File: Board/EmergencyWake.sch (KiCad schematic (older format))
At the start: 129 parts, among them J1 USB_C_Receptacle_USB2.0, J2 Micro_SD_Card_Det, J3 Conn_01x03, J4 Conn_01x02, J5 Conn_01x04, J6 Conn_01x04, J7 Conn_01x02, J8 Conn_01x04, J9 Conn_01x04, Q1 AO3400A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

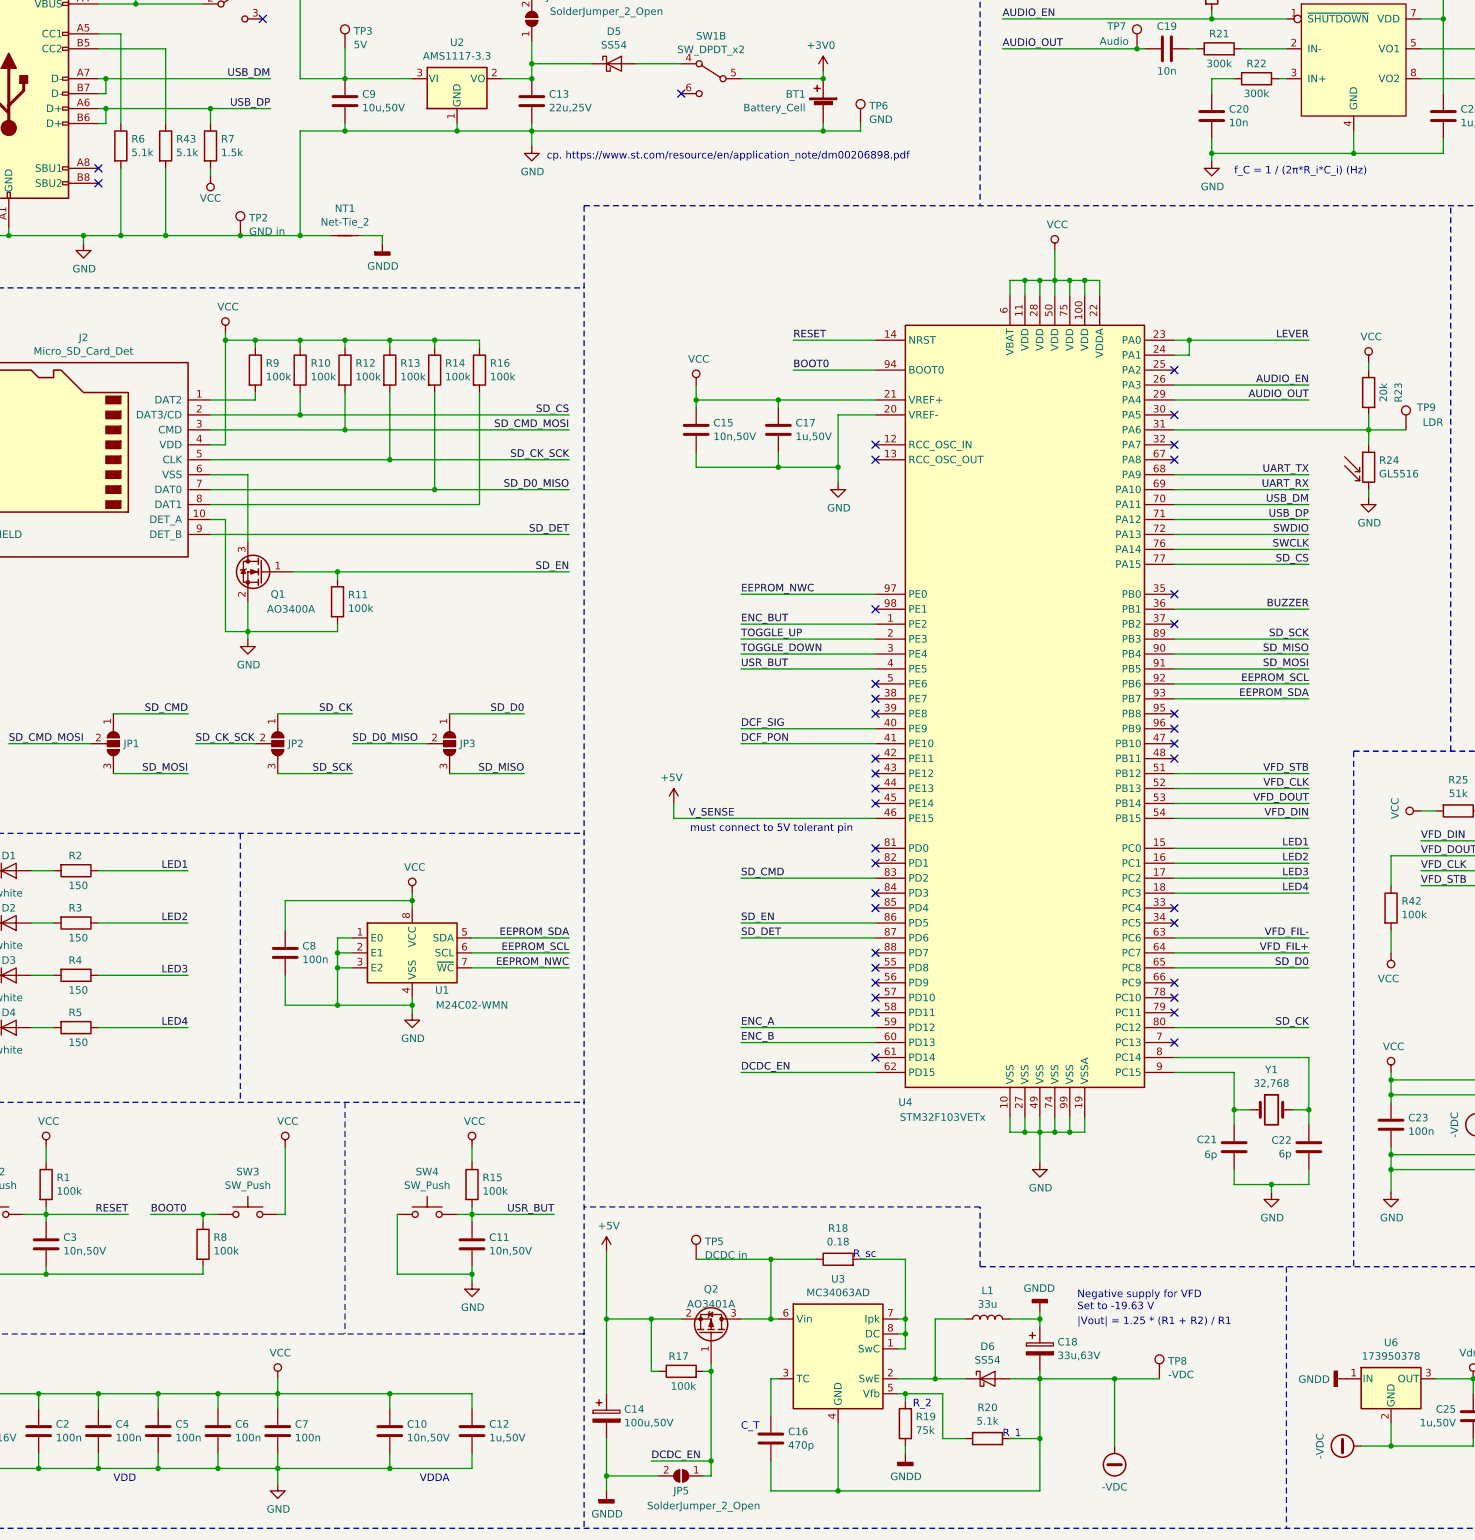
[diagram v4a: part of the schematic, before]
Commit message: [Board] Switched from F103 to F407
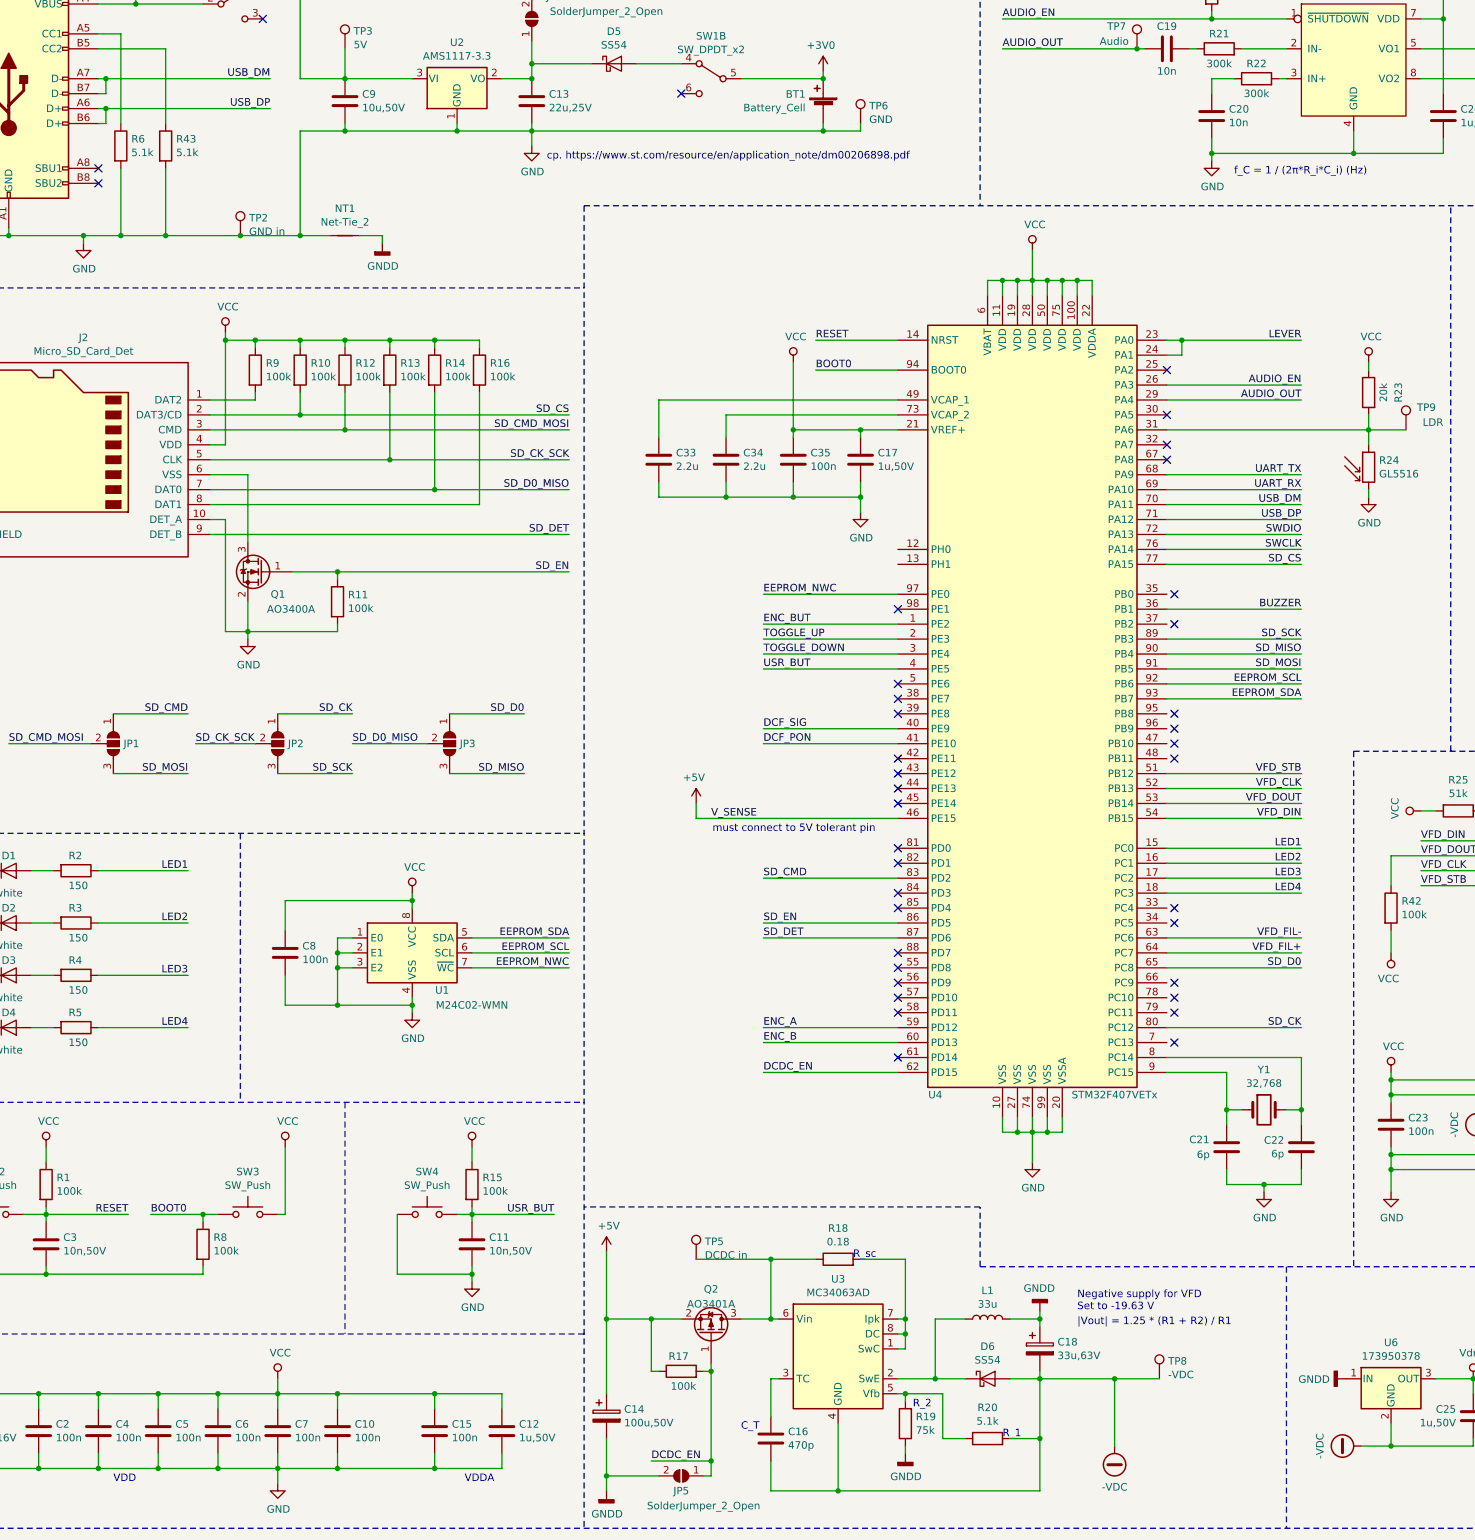
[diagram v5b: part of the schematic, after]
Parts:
- removed R7: 1.5k, Resistor_SMD:R_0603_1608Metric, symbol Device:R
- removed U4: STM32F103VETx, Package_QFP:LQFP-100_14x14mm_P0.5mm, symbol MCU_ST_STM32F1:STM32F103VETx
- added C33, C34: 2.2u, Capacitor_SMD:C_0603_1608Metric, symbol Device:C
- added C35: 100n, Capacitor_SMD:C_0402_1005Metric, symbol Device:C
- added U4: STM32F407VETx, Package_QFP:LQFP-100_14x14mm_P0.5mm, symbol MCU_ST_STM32F4:STM32F407VETx
- C10, C15: value 10n,50V -> 100n; LCSC C15195 -> C1525
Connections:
- net +5V: now also U4.46 (PE15)
- net AUDIO_EN: now also U4.26 (PA3)
- net AUDIO_OUT: now also U4.29 (PA4)
- net BOOT0: now also U4.94 (BOOT0)
- net BUZZER: now also U4.36 (PB1)
- net DCDC_EN: now also U4.62 (PD15)
- net DCF_PON: now also U4.41 (PE10)
- net DCF_SIG: now also U4.40 (PE9)
- net EEPROM_NWC: now also U4.97 (PE0)
- net EEPROM_SCL: now also U4.92 (PB6)
- net EEPROM_SDA: now also U4.93 (PB7)
- net ENC_A: now also U4.59 (PD12)
- net ENC_B: now also U4.60 (PD13)
- net ENC_BUT: now also U4.1 (PE2)
- net GND: now also C33.2, C34.2, C35.2, U4.10 (VSS), U4.20 (VSSA), U4.27 (VSS), U4.74 (VSS), U4.99 (VSS)
- net LED1: now also U4.15 (PC0)
- net LED2: now also U4.16 (PC1)
- net LED3: now also U4.17 (PC2)
- net LED4: now also U4.18 (PC3)
- net LEVER: now also U4.23 (PA0), U4.24 (PA1)
- net RESET: now also U4.14 (NRST)
- net SD_CK: now also U4.80 (PC12)
- net SD_CMD: now also U4.83 (PD2)
- net SD_CS: now also U4.77 (PA15)
- net SD_D0: now also U4.65 (PC8)
- net SD_DET: now also U4.87 (PD6)
- net SD_EN: now also U4.86 (PD5)
- net SD_MISO: now also U4.90 (PB4)
- net SD_MOSI: now also U4.91 (PB5)
- net SD_SCK: now also U4.89 (PB3)
- net SWCLK: now also U4.76 (PA14)
- net SWDIO: now also U4.72 (PA13)
- net TOGGLE_DOWN: now also U4.3 (PE4)
- net TOGGLE_UP: now also U4.2 (PE3)
- net UART_RX: now also U4.69 (PA10)
- net UART_TX: now also U4.68 (PA9)
- net USB_DM: now also U4.70 (PA11)
- net USB_DP: now also U4.71 (PA12)
- net USR_BUT: now also U4.4 (PE5)
- net VCC: now also C35.1, U4.100 (VDD), U4.11 (VDD), U4.19 (VDD), U4.21 (VREF+), U4.22 (VDDA), U4.28 (VDD), U4.50 (VDD), U4.6 (VBAT), U4.75 (VDD)
- net VFD_CLK: now also U4.52 (PB13)
- net VFD_DIN: now also U4.54 (PB15)
- net VFD_DOUT: now also U4.53 (PB14)
- net VFD_FIL+: now also U4.64 (PC7)
- net VFD_FIL-: now also U4.63 (PC6)
- net VFD_STB: now also U4.51 (PB12)
- net at R23.2, R24.1, TP9.1: now also U4.31 (PA6)
- net at C22.1, Y1.2: now also U4.8 (PC14)
- net at C21.1, Y1.1: now also U4.9 (PC15)
- new net: C33.1, U4.49 (VCAP_1)
- new net: C34.1, U4.73 (VCAP_2)
- no-connect marks 58 -> 56
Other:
- moved on the sheet: C12, C17, C21, C22, Y1

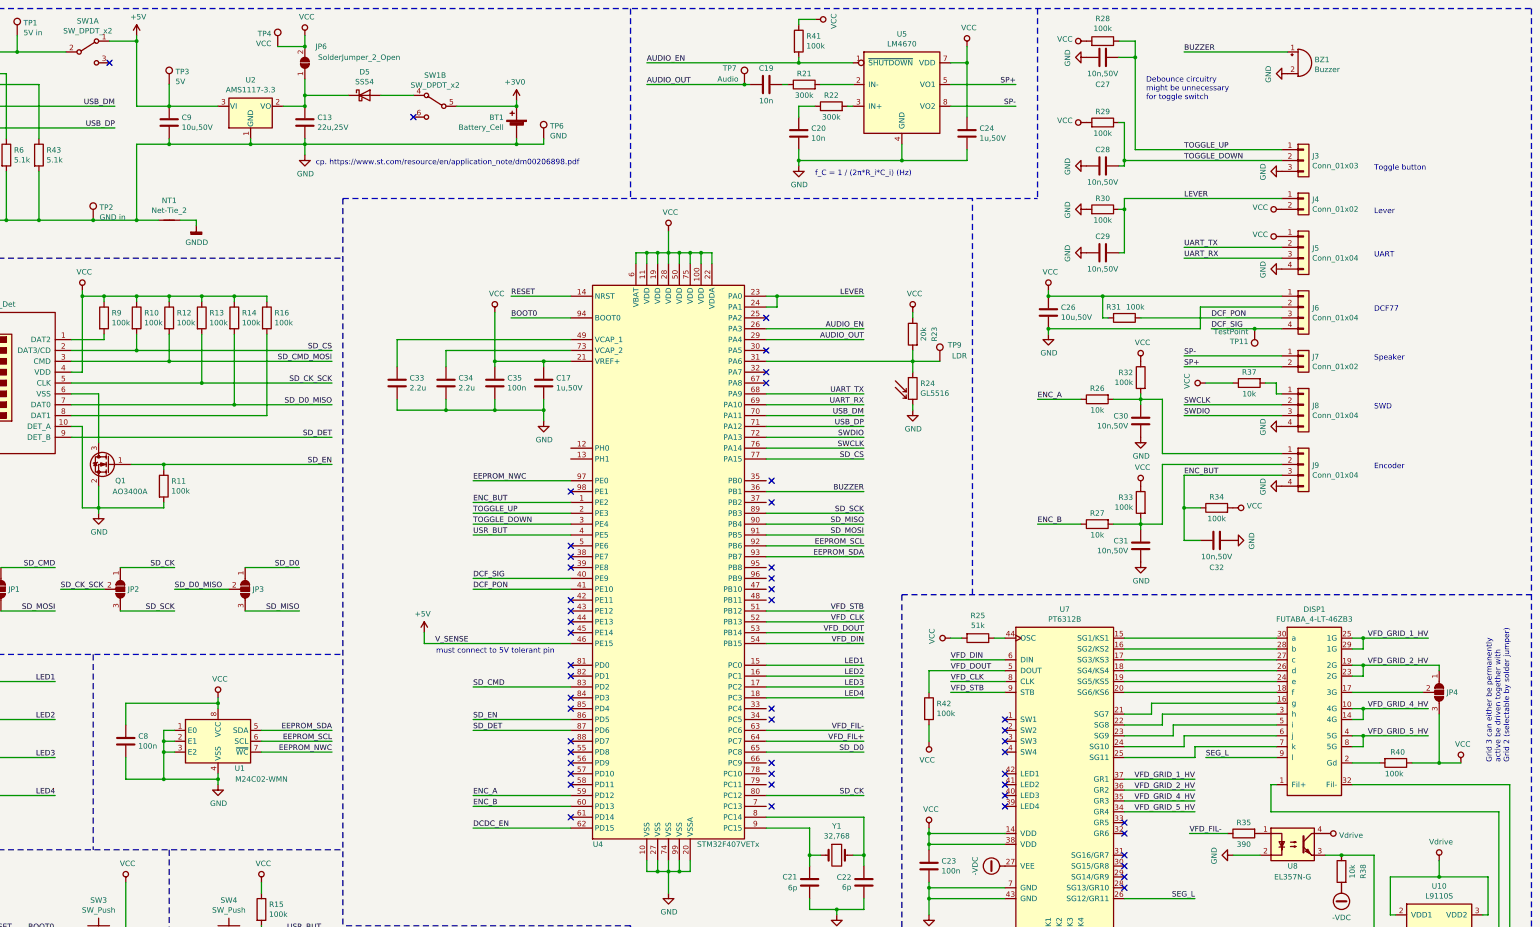
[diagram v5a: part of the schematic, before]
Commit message: [Board] Removed solder paste for not-fitted components. Added I2C for proximity sensor. Moved SWD and UART connector
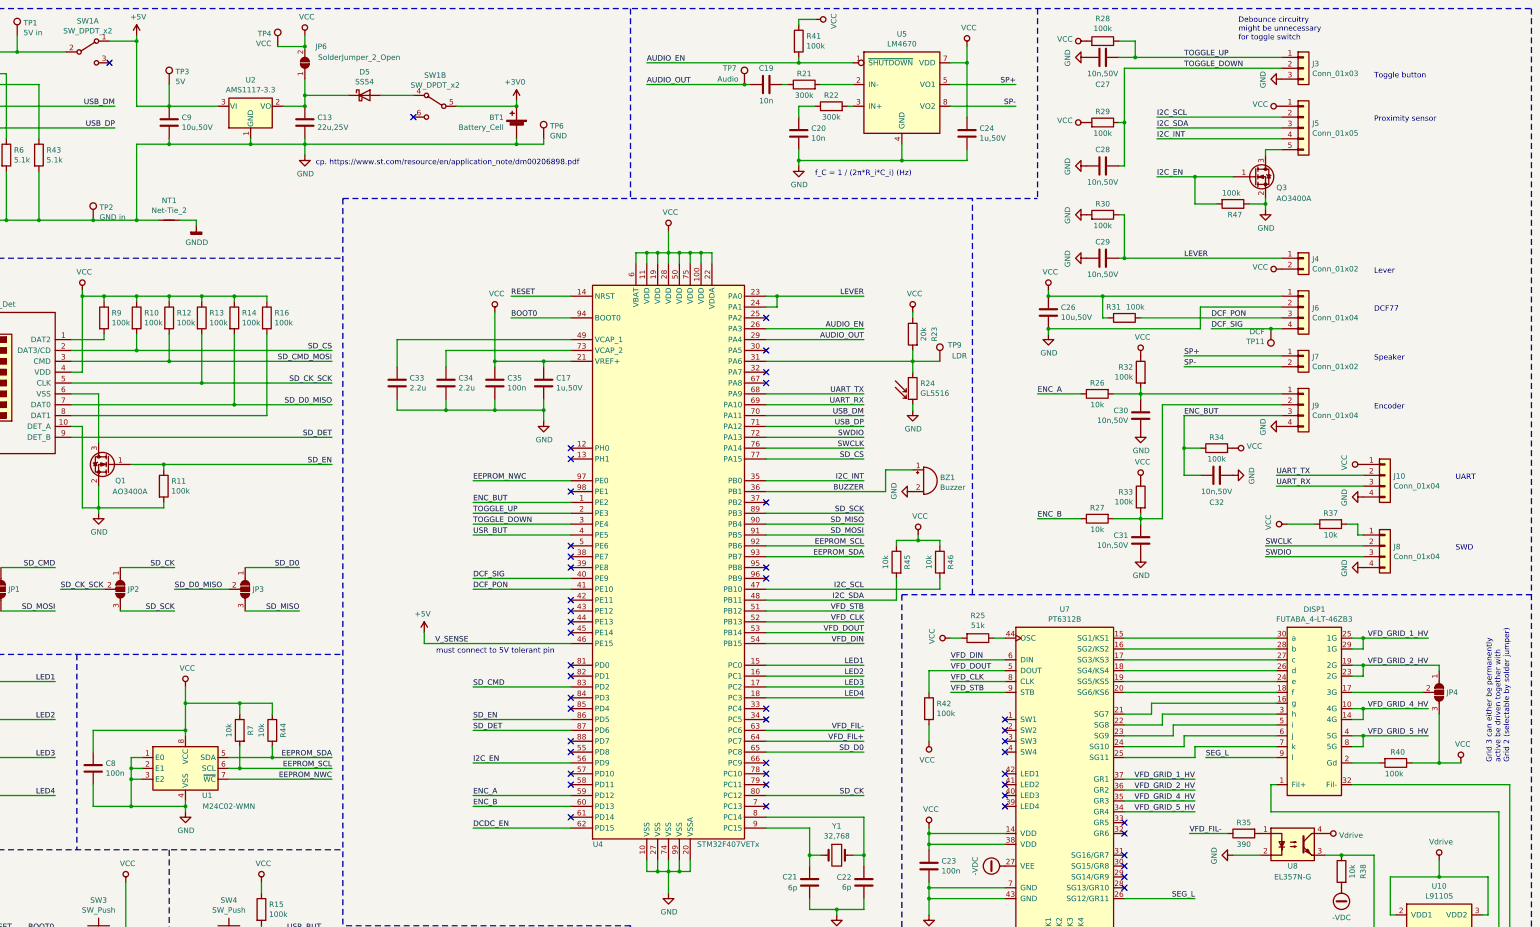
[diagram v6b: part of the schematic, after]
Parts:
- removed J5: Conn_01x04, Connector_PinHeader_2.54mm:PinHeader_1x04_P2.54mm_Horizontal, symbol Connector_Generic:Conn_01x04
- added J10: Conn_01x04, WR-WTB:WR-WTB 2.00mm SMT Male Horizontal Shrouded Header 4 Pins, symbol Connector_Generic:Conn_01x04
- added J5: Conn_01x05, Connector_PinHeader_2.54mm:PinHeader_1x05_P2.54mm_Horizontal, symbol Connector_Generic:Conn_01x05
- added Q3: AO3400A, Package_TO_SOT_SMD:SOT-23, symbol Device:Q_NMOS_GSD
- added R44, R45, R46, R7: 10k, Resistor_SMD:R_0402_1005Metric, symbol Device:R
- added R47: 100k, Resistor_SMD:R_0402_1005Metric, symbol Device:R
- J8: footprint Connector_PinHeader_2.54mm:PinHeader_1x04_P2.54mm_Horizontal -> WR-WTB:WR-WTB 2.00mm SMT Male Horizontal Shrouded Header 4 Pins
- TP11: value TestPoint -> DCF
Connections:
- net EEPROM_SCL: now also R7.2
- net EEPROM_SDA: now also R44.2
- net GND: now also J10.4 (Pin_4), Q3.2 (S), R47.1
- net SP+: now also J7.1 (Pin_1); no longer J7.2 (Pin_2)
- net SP-: now also J7.2 (Pin_2); no longer J7.1 (Pin_1)
- net UART_RX: now also J10.3 (Pin_3)
- net UART_TX: now also J10.2 (Pin_2)
- net VCC: now also J10.1 (Pin_1), J5.1 (Pin_1), R44.1, R45.1, R46.1, R7.1
- net I2C_INT: now reaches U4.35 (PB0)
- net I2C_INT: now also J5.4 (Pin_4)
- net I2C_SCL: now reaches U4.47 (PB10)
- net I2C_SCL: now also J5.2 (Pin_2), R46.2
- net I2C_SDA: now reaches U4.48 (PB11)
- net I2C_SDA: now also J5.3 (Pin_3), R45.2
- net I2C_EN: now reaches U4.56 (PD9)
- net I2C_EN: now also Q3.1 (G), R47.2
- new net: J5.5 (Pin_5), Q3.3 (D)
- no-connect marks 56 -> 54
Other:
- note added: "Proximity sensor"
- moved on the sheet: BZ1, C29, C30, C31, C32, C8, J3, J4, J8, J9, R26, R27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
